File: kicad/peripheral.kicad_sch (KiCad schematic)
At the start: 4 parts, among them J3 Conn_01x13_Socket, U5 MAX17048G+T10

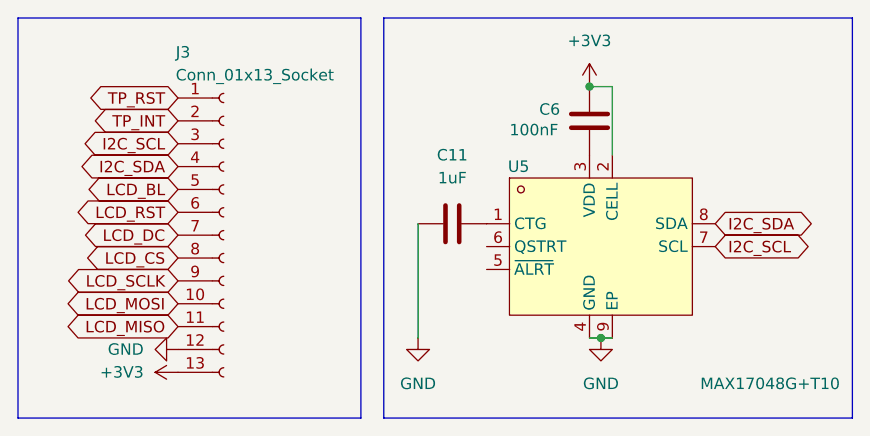
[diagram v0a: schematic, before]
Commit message: fix: rewire MAX17048 CELL pin from +3V3 to +BATT
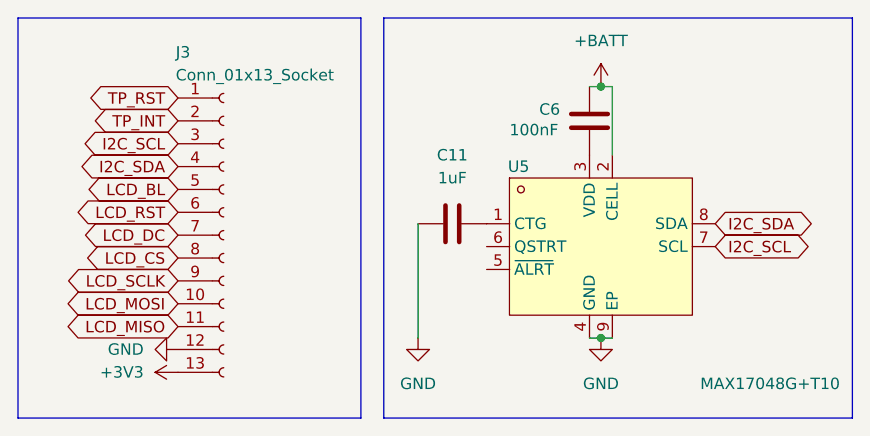
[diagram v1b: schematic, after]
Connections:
- net +3V3: no longer C6.1, U5.2 (CELL)
- new net +BATT: C6.1, U5.2 (CELL)
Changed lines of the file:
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@@
+	)
+	(junction
+		(at 81.28 24.13)
+		(diameter 0)
+		(color 0 0 0 0)
 	)
 	(junction
@@
 		(color 0 0 0 0)
 	)
-	(junction
-		(at 80.01 24.13)
-		(diameter 0)
-		(color 0 0 0 0)
+	(wire
+		(pts
+			(xy 81.28 24.13) (xy 80.01 24.13)
+		)
+		(stroke
+			(width 0)
+			(type default)
+		)
 	)
 	(wire
@@
 	(wire
 		(pts
-			(xy 82.55 24.13) (xy 80.01 24.13)
+			(xy 82.55 24.13) (xy 81.28 24.13)
 		)
 		(stroke
@@
 				(path "/5848c585-af30-4d48-87e3-721d2ec71b1d/06be15b7-7363-4216-94f2-1f997c0531fe"
 					(reference "#PWR030")
+					(unit 1)
+				)
+			)
+		)
+	)
+	(symbol
+		(lib_id "power:+BATT")
+		(at 81.28 24.13 0)
+		(unit 1)
+		(exclude_from_sim no)
+		(in_bom yes)
+		(on_board yes)
+		(dnp no)
+		(fields_autoplaced yes)
+		(property "Reference" "#PWR032"
+			(at 81.28 27.94 0)
+			(effects
+				(font
+					(size 1.27 1.27)
+				)
+				(hide yes)
+			)
+		)
+		(property "Value" "+BATT"
+			(at 81.28 19.05 0)
+			(effects
+				(font
+					(size 1.27 1.27)
+				)
+			)
+		)
+		(property "Footprint" ""
+			(at 81.28 24.13 0)
+			(effects
+				(font
+					(size 1.27 1.27)
+				)
+				(hide yes)
+			)
+		)
+		(property "Datasheet" ""
+			(at 81.28 24.13 0)
+			(effects
+				(font
+					(size 1.27 1.27)
+				)
+				(hide yes)
+			)
+		)
+		(property "Description" "Power symbol creates a global label with name \"+BATT\""
+			(at 81.28 24.13 0)
+			(effects
+				(font
+					(size 1.27 1.27)
+				)
+				(hide yes)
+			)
+		)
+		(pin "1"
+		)
+		(instances
+			(project ""
+				(path "/5848c585-af30-4d48-87e3-721d2ec71b1d/06be15b7-7363-4216-94f2-1f997c0531fe"
+					(reference "#PWR032")
 					(unit 1)
 				)
@@
 					(unit 1)
 				)
-			)
-		)
-	)
-	(symbol
-		(lib_id "power:+3V3")
-		(at 80.01 24.13 0)
-		(unit 1)
-		(exclude_from_sim no)
-		(in_bom yes)
-		(on_board yes)
-		(dnp no)
-		(fields_autoplaced yes)
-		(property "Reference" "#PWR032"
-			(at 80.01 27.94 0)
-			(effects
-				(font
-					(size 1.27 1.27)
-				)
-				(hide yes)
-			)
-		)
-		(property "Value" "+3V3"
-			(at 80.01 19.05 0)
-			(effects
-				(font
-					(size 1.27 1.27)
-				)
-			)
-		)
-		(property "Footprint" ""
-			(at 80.01 24.13 0)
-			(effects
-				(font
-					(size 1.27 1.27)
-				)
-				(hide yes)
-			)
-		)
-		(property "Datasheet" ""
-			(at 80.01 24.13 0)
-			(effects
-				(font
-					(size 1.27 1.27)
-				)
-				(hide yes)
-			)
-		)
-		(property "Description" "Power symbol creates a global label with name \"+3V3\""
-			(at 80.01 24.13 0)
-			(effects
-				(font
-					(size 1.27 1.27)
-				)
-				(hide yes)
-			)
-		)
-		(pin "1"
-		)
-		(instances
-			(project "VRCBadge"
-				(path "/5848c585-af30-4d48-87e3-721d2ec71b1d/06be15b7-7363-4216-94f2-1f997c0531fe"
-					(reference "#PWR032")
-					(unit 1)
-				)
